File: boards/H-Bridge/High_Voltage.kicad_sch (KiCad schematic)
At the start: 22 parts, among them IC2 MIC4606-1YML-TR, IC3 AD8410AWBRZ-RL, J1 V+, J2 V-, J3 Motor-, J4 Motor+, J9 12V+, M1 Motor_DC, Q1 NTBLS4D0N15MC, Q2 NTBLS4D0N15MC, Q3 NTBLS4D0N15MC, Q4 NTBLS4D0N15MC

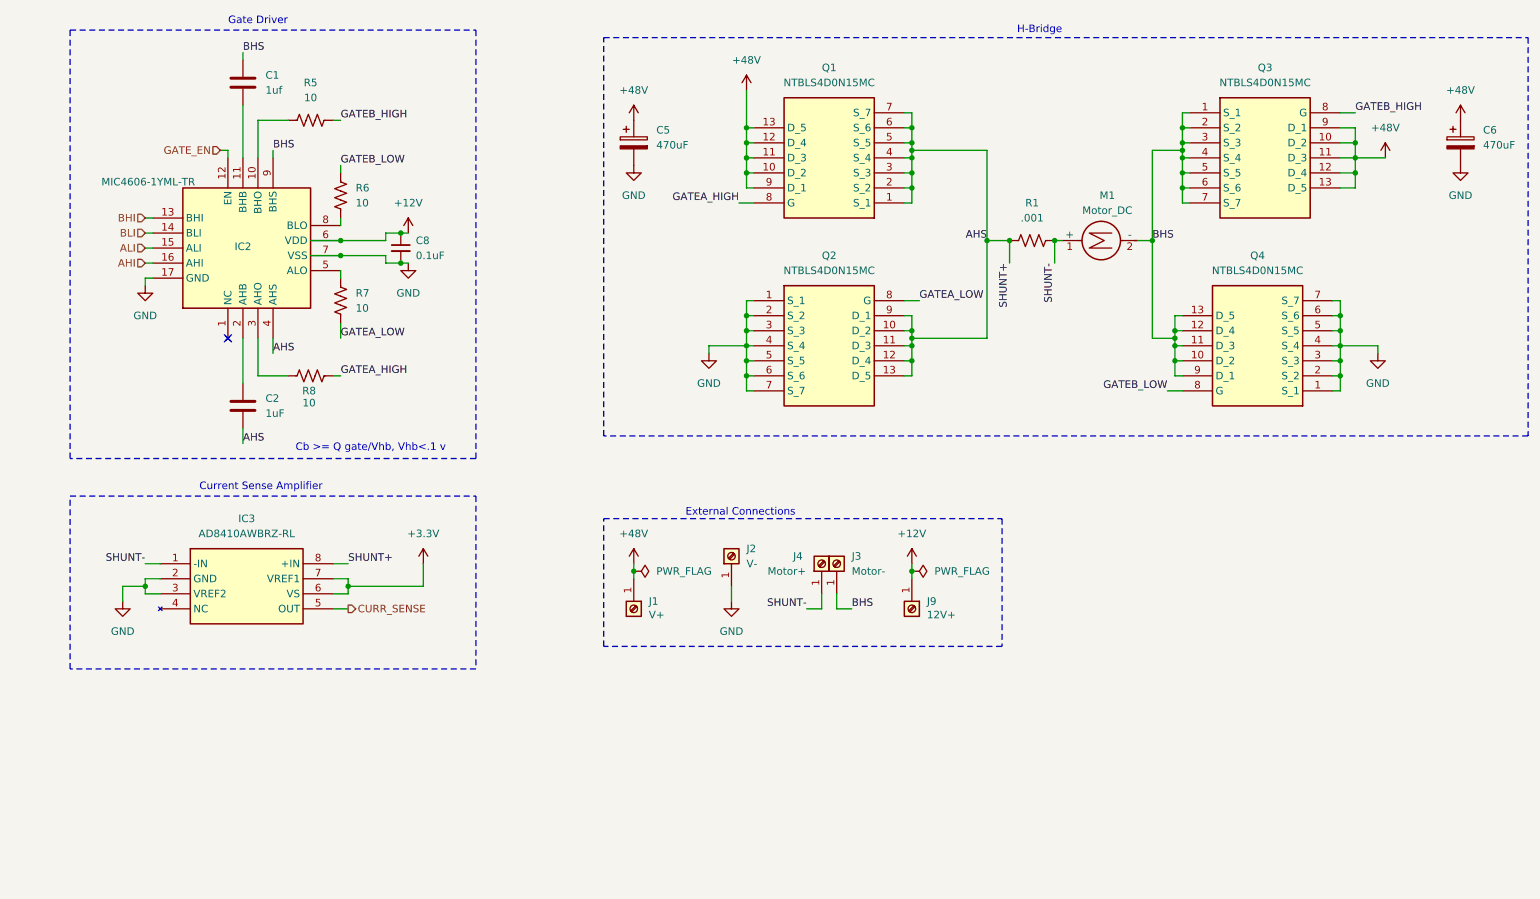
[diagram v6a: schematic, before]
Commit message: added negative voltage per h-bridge docs
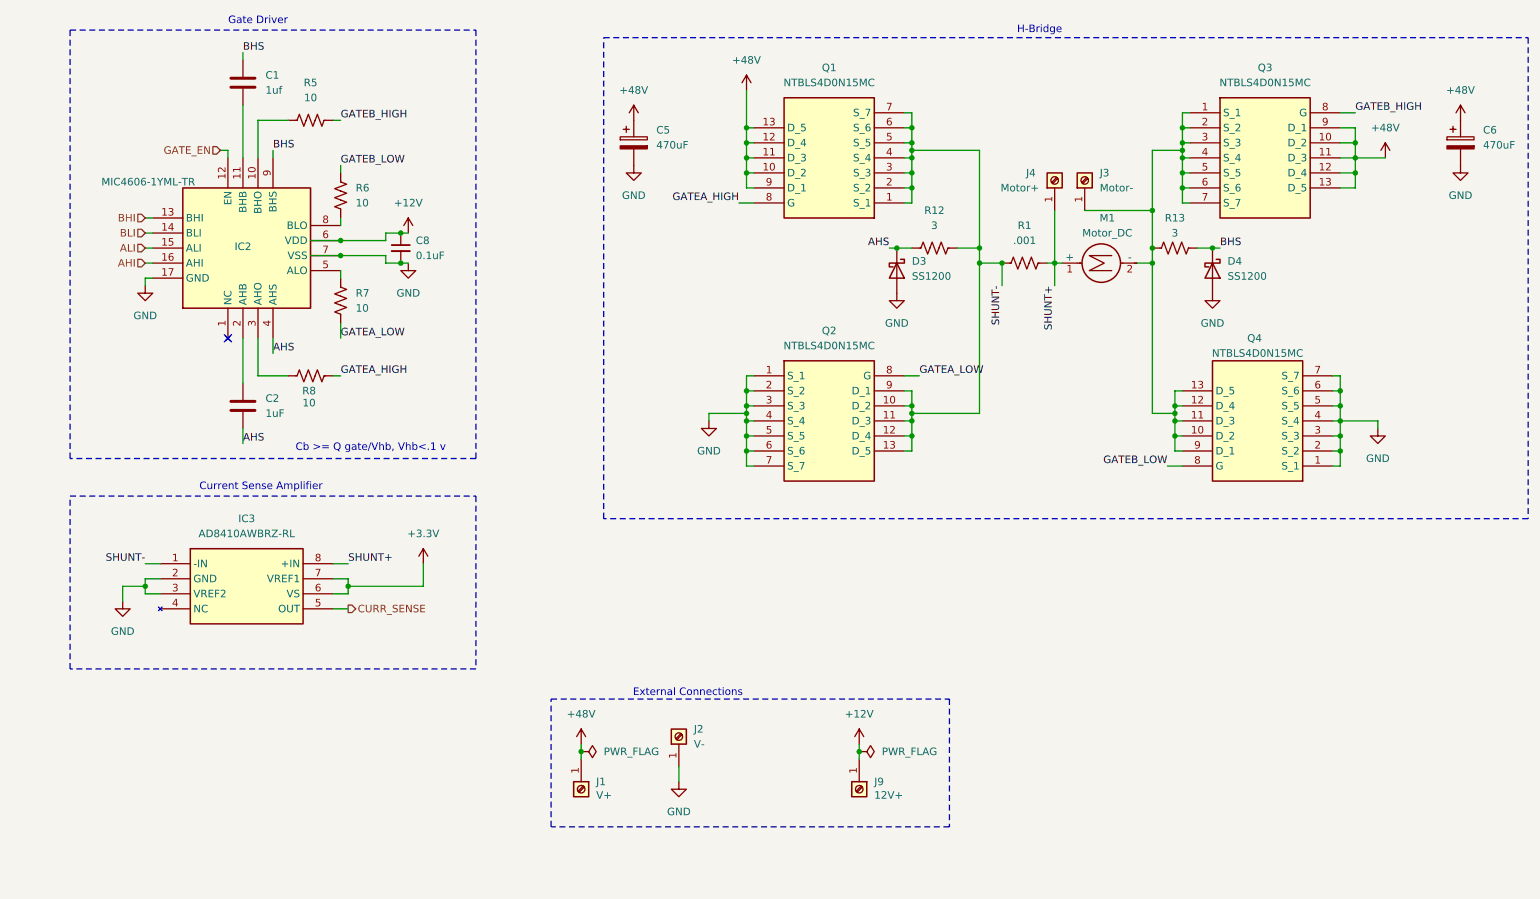
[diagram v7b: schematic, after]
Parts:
- added D3, D4: SS1200, Diode_SMD:D_SMA, symbol Diode:SS1200
- added R12, R13: 3, Resistor_SMD:R_0603_1608Metric, symbol Device:R_US
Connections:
- net AHS: now also D3.1 (K), R12.2; no longer IC3.8 (+IN), Q1.1 (S_1), Q1.2 (S_2), Q1.3 (S_3), Q1.4 (S_4), Q1.5 (S_5), Q1.6 (S_6), Q1.7 (S_7), Q2.10 (D_2), Q2.11 (D_3), Q2.12 (D_4), Q2.13 (D_5), Q2.9 (D_1), R1.1
- net BHS: now also D4.1 (K), R13.1; no longer J3.1 (Pin_1), M1.2 (-), Q3.1 (S_1), Q3.2 (S_2), Q3.3 (S_3), Q3.4 (S_4), Q3.5 (S_5), Q3.6 (S_6), Q3.7 (S_7), Q4.10 (D_2), Q4.11 (D_3), Q4.12 (D_4), Q4.13 (D_5), Q4.9 (D_1)
- net GND: now also D3.2 (A), D4.2 (A)
- net SHUNT-: now also Q1.1 (S_1), Q1.2 (S_2), Q1.3 (S_3), Q1.4 (S_4), Q1.5 (S_5), Q1.6 (S_6), Q1.7 (S_7), Q2.10 (D_2), Q2.11 (D_3), Q2.12 (D_4), Q2.13 (D_5), Q2.9 (D_1), R1.1, R12.1; no longer J4.1 (Pin_1), M1.1 (+), R1.2
- new net: J3.1 (Pin_1), M1.2 (-), Q3.1 (S_1), Q3.2 (S_2), Q3.3 (S_3), Q3.4 (S_4), Q3.5 (S_5), Q3.6 (S_6), Q3.7 (S_7), Q4.10 (D_2), Q4.11 (D_3), Q4.12 (D_4), Q4.13 (D_5), Q4.9 (D_1), R13.2
- new net SHUNT+: IC3.8 (+IN), J4.1 (Pin_1), M1.1 (+), R1.2
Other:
- moved on the sheet: J1, J2, J9, M1, Q2, Q4, R1
